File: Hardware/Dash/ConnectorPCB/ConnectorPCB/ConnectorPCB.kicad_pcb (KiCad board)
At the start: 2 copper layers, 44.8 x 43.8 mm, 3 parts, among them J1 776276-1, J2 2.54mm 1x4, J3 2.54mm 1x4

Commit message: PCB R0.1.0
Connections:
- J1 pad 4: CAN_H -> GND
- J1 pad 6: GND -> CAN_H
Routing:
- net GND: track 15.3 -> 26.6 mm
- net CAN_H: track 28.3 -> 29.3 mm
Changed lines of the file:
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@@
       (net 3 "WAKE_UP") (pinfunction "3") (pintype "passive"))
     (pad "4" thru_hole circle (at 2 4) (size 2.625 2.625) (drill 1.75) (layers "*.Cu" "*.Mask")
-      (net 4 "CAN_H") (pinfunction "4") (pintype "passive"))
+      (net 6 "GND") (pinfunction "4") (pintype "passive"))
     (pad "5" thru_hole circle (at 6 4) (size 2.625 2.625) (drill 1.75) (layers "*.Cu" "*.Mask")
       (net 5 "CAN_L") (pinfunction "5") (pintype "passive"))
     (pad "6" thru_hole circle (at 0 8) (size 2.625 2.625) (drill 1.75) (layers "*.Cu" "*.Mask")
-      (net 6 "GND") (pinfunction "6") (pintype "passive"))
+      (net 4 "CAN_H") (pinfunction "6") (pintype "passive"))
     (pad "7" thru_hole circle (at 4 8) (size 2.625 2.625) (drill 1.75) (layers "*.Cu" "*.Mask")
       (net 7 "D+") (pinfunction "7") (pintype "passive"))
@@
     (stroke (width 0.1) (type default)) (layer "Edge.Cuts"))
   (segment (start 141.275 58.925) (end 141.7 58.5) (width 0.8) (layer "F.Cu") (net 1))
-  (segment (start 141.275 73.755) (end 141.275 58.925) (width 0.8) (layer "F.Cu") (net 1))
+  (segment (start 141.275 73.755) (end 141.275 58.925) (width 1.5) (layer "F.Cu") (net 1))
   (segment (start 144.24 71.74) (end 144.24 58.5) (width 0.8) (layer "F.Cu") (net 2))
   (segment (start 144.25 71.75) (end 144.24 71.74) (width 0.8) (layer "F.Cu") (net 2))
@@
   (segment (start 149.275 73.755) (end 146.75 71.23) (width 0.8) (layer "F.Cu") (net 3))
   (segment (start 146.75 71.23) (end 146.75 70) (width 0.8) (layer "F.Cu") (net 3))
-  (segment (start 145.75 64) (end 145.75 62.07) (width 0.8) (layer "B.Cu") (net 4))
-  (segment (start 143.275 77.755) (end 141.801472 77.755) (width 0.8) (layer "B.Cu") (net 4))
-  (segment (start 137.75 75.5) (end 137.75 72) (width 0.8) (layer "B.Cu") (net 4))
-  (segment (start 138.5 76.25) (end 137.75 75.5) (width 0.8) (layer "B.Cu") (net 4))
-  (segment (start 141.801472 77.755) (end 140.296472 76.25) (width 0.8) (layer "B.Cu") (net 4))
-  (segment (start 140.296472 76.25) (end 138.5 76.25) (width 0.8) (layer "B.Cu") (net 4))
-  (segment (start 137.75 72) (end 145.75 64) (width 0.8) (layer "B.Cu") (net 4))
-  (segment (start 145.75 62.07) (end 149.32 58.5) (width 0.8) (layer "B.Cu") (net 4))
+  (segment (start 141.42 81.9) (end 141.275 81.755) (width 0.8) (layer "F.Cu") (net 4))
+  (segment (start 138.225 78.705) (end 138.225 69.595) (width 0.8) (layer "B.Cu") (net 4))
+  (segment (start 141.275 81.755) (end 138.225 78.705) (width 0.8) (layer "B.Cu") (net 4))
+  (segment (start 138.225 69.595) (end 149.32 58.5) (width 0.8) (layer "B.Cu") (net 4))
   (segment (start 152 81.1675) (end 152 94.04) (width 0.8) (layer "F.Cu") (net 5))
   (segment (start 147.275 77.755) (end 148.5875 77.755) (width 0.8) (layer "F.Cu") (net 5))
   (segment (start 152 94.04) (end 149.04 97) (width 0.8) (layer "F.Cu") (net 5))
   (segment (start 148.5875 77.755) (end 152 81.1675) (width 0.8) (layer "F.Cu") (net 5))
-  (segment (start 141.42 81.9) (end 141.275 81.755) (width 0.8) (layer "F.Cu") (net 6))
-  (segment (start 141.42 97) (end 141.42 81.9) (width 0.8) (layer "F.Cu") (net 6))
+  (segment (start 141.42 93.17) (end 141.42 97) (width 1.5) (layer "F.Cu") (net 6))
+  (segment (start 138.645 77.755) (end 136.75 79.65) (width 1.5) (layer "F.Cu") (net 6))
+  (segment (start 136.75 79.65) (end 136.75 88.5) (width 1.5) (layer "F.Cu") (net 6))
+  (segment (start 143.275 77.755) (end 138.645 77.755) (width 1.5) (layer "F.Cu") (net 6))
+  (segment (start 136.75 88.5) (end 141.42 93.17) (width 1.5) (layer "F.Cu") (net 6))
   (via (at 145.5 69) (size 0.5) (drill 0.3) (layers "F.Cu" "B.Cu") (free) (net 6))
   (via (at 149.5 89.25) (size 0.5) (drill 0.3) (layers "F.Cu" "B.Cu") (free) (net 6))

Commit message: :adhesive_bandage: Minor change to the PCB
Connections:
- J2 pad 4: CAN_H -> GND
- J3 pad 4: GND -> CAN_H
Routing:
- net CAN_H: track 29.3 -> 15.5 mm
- net GND: track 26.6 -> 30.5 mm
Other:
- outline, holes or cut-outs redrawn
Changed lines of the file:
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@@
       (net 3 "WAKE_UP") (pintype "passive"))
     (pad "4" thru_hole oval (at 0 -7.62 270) (size 1.7 1.7) (drill 1) (layers "*.Cu" "*.Mask")
-      (net 4 "CAN_H") (pintype "passive"))
+      (net 6 "GND") (pintype "passive"))
     (model "${KICAD6_3DMODEL_DIR}/Connector_PinHeader_2.54mm.3dshapes/PinHeader_1x04_P2.54mm_Vertical.wrl"
       (offset (xyz 0 0 0))
@@
       (net 7 "D+") (pintype "passive"))
     (pad "4" thru_hole oval (at 0 -7.62 90) (size 1.7 1.7) (drill 1) (layers "*.Cu" "*.Mask")
-      (net 6 "GND") (pintype "passive"))
+      (net 4 "CAN_H") (pintype "passive"))
     (model "${KICAD6_3DMODEL_DIR}/Connector_PinHeader_2.54mm.3dshapes/PinHeader_1x04_P2.54mm_Vertical.wrl"
       (offset (xyz 0 0 0))
@@
     )
   )
-  (gr_line (start 122.75 95.5) (end 122.75 60)
+  (gr_arc (start 154.75 60) (mid 153.335786 59.414214) (end 152.75 58)
     (stroke (width 0.1) (type default)) (layer "Edge.Cuts"))
-  (gr_line (start 138.25 56) (end 152.75 56)
+  (gr_line (start 122.75 93.5) (end 122.75 62)
     (stroke (width 0.1) (type default)) (layer "Edge.Cuts"))
-  (gr_line (start 138 95.5) (end 122.75 95.5)
+  (gr_arc (start 167.5 93.5) (mid 166.914214 94.914214) (end 165.5 95.5)
     (stroke (width 0.1) (type default)) (layer "Edge.Cuts"))
-  (gr_line (start 152.75 56) (end 152.75 60)
+  (gr_line (start 140.25 56) (end 150.75 56)
     (stroke (width 0.1) (type default)) (layer "Edge.Cuts"))
-  (gr_line (start 167.5 95.5) (end 167.5 60)
+  (gr_arc (start 138.25 58) (mid 138.835786 56.585786) (end 140.25 56)
     (stroke (width 0.1) (type default)) (layer "Edge.Cuts"))
-  (gr_line (start 152.75 60) (end 167.5 60)
+  (gr_arc (start 152.5 97.75) (mid 151.914214 99.164214) (end 150.5 99.75)
     (stroke (width 0.1) (type default)) (layer "Edge.Cuts"))
-  (gr_line (start 152.5 95.5) (end 167.5 95.5)
+  (gr_arc (start 150.75 56) (mid 152.164214 56.585786) (end 152.75 58)
     (stroke (width 0.1) (type default)) (layer "Edge.Cuts"))
-  (gr_line (start 138.25 60) (end 122.75 60)
+  (gr_arc (start 165.5 60) (mid 166.914214 60.585786) (end 167.5 62)
     (stroke (width 0.1) (type default)) (layer "Edge.Cuts"))
-  (gr_line (start 138 95.5) (end 138 99.75)
+  (gr_arc (start 138.25 58) (mid 137.664214 59.414214) (end 136.25 60)
     (stroke (width 0.1) (type default)) (layer "Edge.Cuts"))
-  (gr_line (start 138.25 60) (end 138.25 56)
+  (gr_line (start 136 95.5) (end 124.75 95.5)
     (stroke (width 0.1) (type default)) (layer "Edge.Cuts"))
-  (gr_line (start 138 99.75) (end 152.5 99.75)
+  (gr_line (start 152.75 58) (end 152.75 58)
     (stroke (width 0.1) (type default)) (layer "Edge.Cuts"))
-  (gr_line (start 152.5 99.75) (end 152.5 95.5)
+  (gr_arc (start 122.75 62) (mid 123.335786 60.585786) (end 124.75 60)
     (stroke (width 0.1) (type default)) (layer "Edge.Cuts"))
-  (segment (start 141.275 58.925) (end 141.7 58.5) (width 0.8) (layer "F.Cu") (net 1))
+  (gr_arc (start 152.5 97.5) (mid 153.085786 96.085786) (end 154.5 95.5)
+    (stroke (width 0.1) (type default)) (layer "Edge.Cuts"))
+  (gr_line (start 167.5 93.5) (end 167.5 62)
+    (stroke (width 0.1) (type default)) (layer "Edge.Cuts"))
+  (gr_line (start 154.75 60) (end 165.5 60)
+    (stroke (width 0.1) (type default)) (layer "Edge.Cuts"))
+  (gr_line (start 154.5 95.5) (end 165.5 95.5)
+    (stroke (width 0.1) (type default)) (layer "Edge.Cuts"))
+  (gr_line (start 136.25 60) (end 124.75 60)
+    (stroke (width 0.1) (type default)) (layer "Edge.Cuts"))
+  (gr_line (start 138 97.5) (end 138 97.75)
+    (stroke (width 0.1) (type default)) (layer "Edge.Cuts"))
+  (gr_arc (start 124.75 95.5) (mid 123.335786 94.914214) (end 122.75 93.5)
+    (stroke (width 0.1) (type default)) (layer "Edge.Cuts"))
+  (gr_line (start 138.25 58) (end 138.25 58)
+    (stroke (width 0.1) (type default)) (layer "Edge.Cuts"))
+  (gr_arc (start 140 99.75) (mid 138.585786 99.164214) (end 138 97.75)
+    (stroke (width 0.1) (type default)) (layer "Edge.Cuts"))
+  (gr_line (start 140 99.75) (end 150.5 99.75)
+    (stroke (width 0.1) (type default)) (layer "Edge.Cuts"))
+  (gr_arc (start 136 95.5) (mid 137.414214 96.085786) (end 138 97.5)
+    (stroke (width 0.1) (type default)) (layer "Edge.Cuts"))
+  (gr_line (start 152.5 97.75) (end 152.5 97.5)
+    (stroke (width 0.1) (type default)) (layer "Edge.Cuts"))
+  (segment (start 141.275 58.925) (end 141.7 58.5) (width 1.5) (layer "F.Cu") (net 1))
   (segment (start 141.275 73.755) (end 141.275 58.925) (width 1.5) (layer "F.Cu") (net 1))
   (segment (start 144.24 71.74) (end 144.24 58.5) (width 0.8) (layer "F.Cu") (net 2))
@@
   (segment (start 149.275 73.755) (end 146.75 71.23) (width 0.8) (layer "F.Cu") (net 3))
   (segment (start 146.75 71.23) (end 146.75 70) (width 0.8) (layer "F.Cu") (net 3))
+  (segment (start 141.275 96.855) (end 141.42 97) (width 0.8) (layer "F.Cu") (net 4))
   (segment (start 141.42 81.9) (end 141.275 81.755) (width 0.8) (layer "F.Cu") (net 4))
-  (segment (start 138.225 78.705) (end 138.225 69.595) (width 0.8) (layer "B.Cu") (net 4))
-  (segment (start 141.275 81.755) (end 138.225 78.705) (width 0.8) (layer "B.Cu") (net 4))
-  (segment (start 138.225 69.595) (end 149.32 58.5) (width 0.8) (layer "B.Cu") (net 4))
+  (segment (start 141.275 81.755) (end 141.275 96.855) (width 0.8) (layer "F.Cu") (net 4))
   (segment (start 152 81.1675) (end 152 94.04) (width 0.8) (layer "F.Cu") (net 5))
   (segment (start 147.275 77.755) (end 148.5875 77.755) (width 0.8) (layer "F.Cu") (net 5))
   (segment (start 152 94.04) (end 149.04 97) (width 0.8) (layer "F.Cu") (net 5))
   (segment (start 148.5875 77.755) (end 152 81.1675) (width 0.8) (layer "F.Cu") (net 5))
-  (segment (start 141.42 93.17) (end 141.42 97) (width 1.5) (layer "F.Cu") (net 6))
-  (segment (start 138.645 77.755) (end 136.75 79.65) (width 1.5) (layer "F.Cu") (net 6))
-  (segment (start 136.75 79.65) (end 136.75 88.5) (width 1.5) (layer "F.Cu") (net 6))
-  (segment (start 143.275 77.755) (end 138.645 77.755) (width 1.5) (layer "F.Cu") (net 6))
-  (segment (start 136.75 88.5) (end 141.42 93.17) (width 1.5) (layer "F.Cu") (net 6))
   (via (at 145.5 69) (size 0.5) (drill 0.3) (layers "F.Cu" "B.Cu") (free) (net 6))
   (via (at 149.5 89.25) (size 0.5) (drill 0.3) (layers "F.Cu" "B.Cu") (free) (net 6))
+  (segment (start 137.755 77.755) (end 136.625 76.625) (width 1.5) (layer "B.Cu") (net 6))
+  (segment (start 141.801472 77.755) (end 137.755 77.755) (width 1.5) (layer "B.Cu") (net 6))
+  (segment (start 136.625 72.525) (end 149.32 59.83) (width 1.5) (layer "B.Cu") (net 6))
+  (segment (start 143.275 77.755) (end 141.801472 77.755) (width 0.8) (layer "B.Cu") (net 6))
+  (segment (start 136.625 76.625) (end 136.625 72.525) (width 1.5) (layer "B.Cu") (net 6))
+  (segment (start 149.32 59.83) (end 149.32 58.5) (width 1.5) (layer "B.Cu") (net 6))
   (segment (start 143.96 97) (end 145.275 95.685) (width 0.8) (layer "F.Cu") (net 7))
   (segment (start 145.275 95.685) (end 145.275 81.755) (width 0.8) (layer "F.Cu") (net 7))

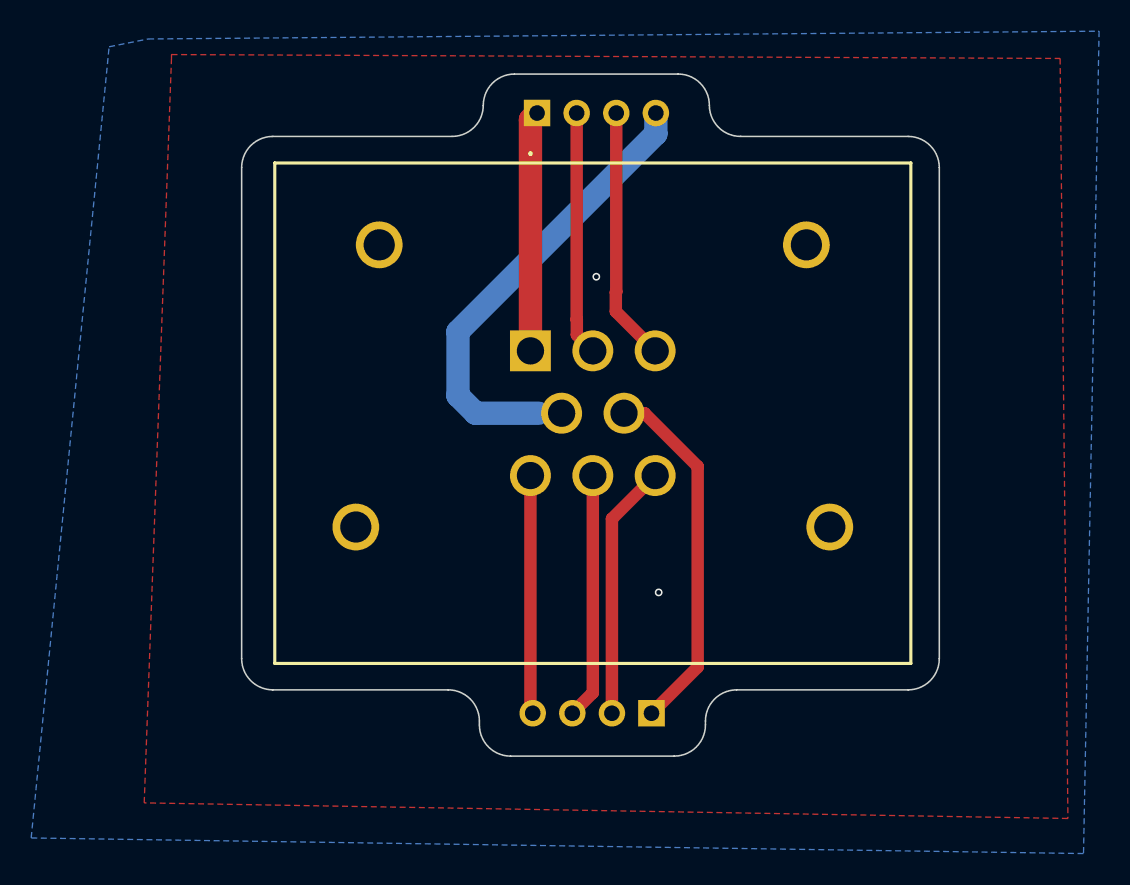
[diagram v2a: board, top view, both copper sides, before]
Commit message: :bug: [FIX] Added space to access the display connector without desoldering the main connector
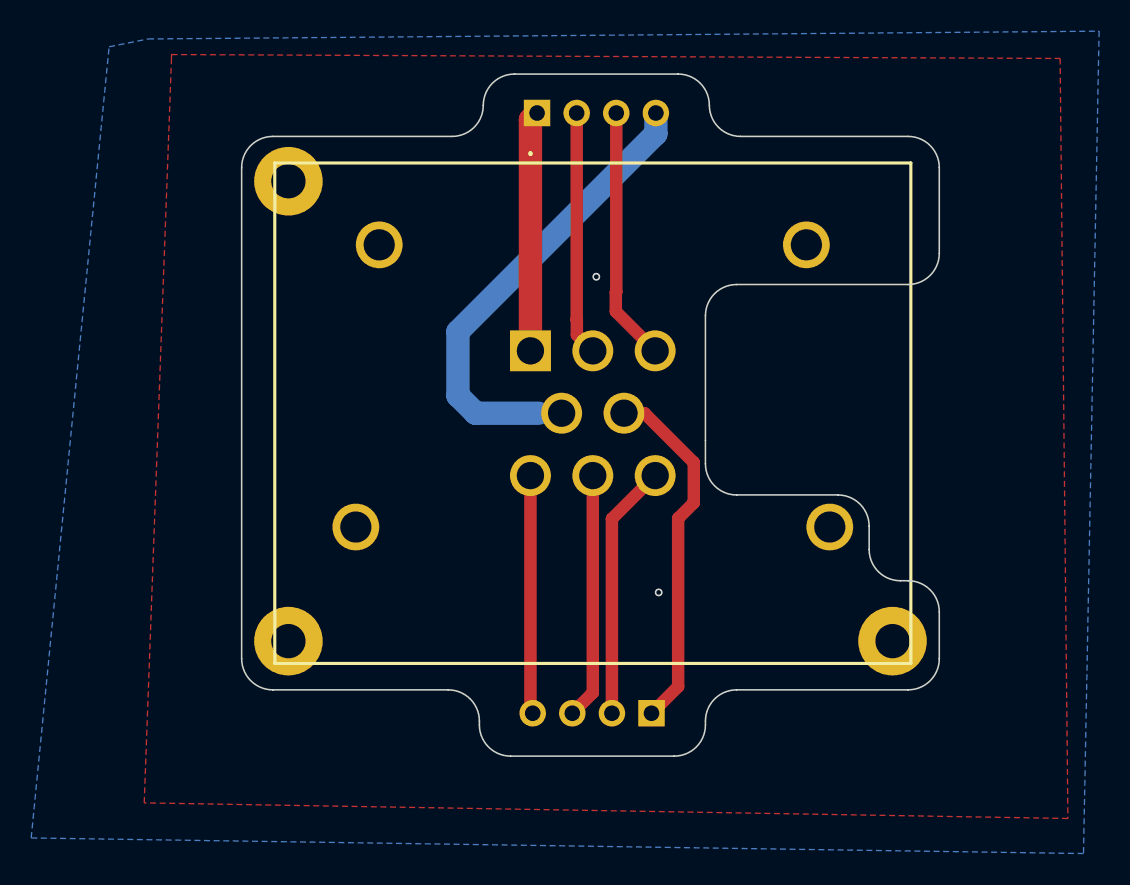
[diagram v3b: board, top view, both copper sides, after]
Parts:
- added ?: , , F.Cu at (164.5, 92.4)
- added ?: , , F.Cu at (125.8, 92.4)
- added H5: MountingHole_Pad, MountingHole:MountingHole_2.2mm_M2_Pad, F.Cu at (125.8, 62.9)
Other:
- outline, holes or cut-outs redrawn
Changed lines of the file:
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@@
     )
+  )
+  (footprint "MountingHole:MountingHole_2.2mm_M2_Pad" (layer "F.Cu")
+    (at 125.75 62.875)
+    (descr "Mounting Hole 2.2mm, M2")
+    (tags "mounting hole 2.2mm m2")
+    (property "LCSC" "C3020128")
+    (property "MOUSER" "")
+    (property "Sheetfile" "connector.kicad_sch")
+    (property "Sheetname" "Connector")
+    (property "ki_description" "Mounting Hole with connection")
+    (property "ki_keywords" "mounting hole")
+    (attr exclude_from_pos_files)
+    (fp_text reference "H5" (at 0 -3.2) (layer "F.SilkS") hide
+        (effects (font (size 1 1) (thickness 0.15)))
+    )
+    (fp_text value "MountingHole_Pad" (at 0 3.2) (layer "F.Fab") hide
+        (effects (font (size 1 1) (thickness 0.15)))
+    )
+    (fp_text user "${REFERENCE}" (at 0 0) (layer "F.Fab")
+        (effects (font (size 1 1) (thickness 0.15)))
+    )
+    (fp_circle (center 0 0) (end 2.2 0)
+      (stroke (width 0.15) (type solid)) (fill none) (layer "Cmts.User"))
+    (fp_circle (center 0 0) (end 2.45 0)
+      (stroke (width 0.05) (type solid)) (fill none) (layer "F.CrtYd"))
+    (pad "1" thru_hole circle (at 0 0) (size 4.4 4.4) (drill 2.2) (layers "*.Cu" "*.Mask")
+      (net 6 "GND") (pinfunction "1") (pintype "input"))
+  )
+  (footprint "" (layer "F.Cu")
+    (at 164.5 92.375)
+    (fp_text reference "" (at 0 0) (layer "F.SilkS")
+        (effects (font (size 1.27 1.27) (thickness 0.15)))
+    )
+    (fp_text value "" (at 0 0) (layer "F.SilkS")
+        (effects (font (size 1.27 1.27) (thickness 0.15)))
+    )
+    (pad "1" thru_hole circle (at 0 0) (size 4.4 4.4) (drill 2.2) (layers "*.Cu" "*.Mask")
+      (net 6 "GND") (pinfunction "1") (pintype "input"))
+  )
+  (footprint "" (layer "F.Cu")
+    (at 125.75 92.375)
+    (fp_text reference "" (at 0 0) (layer "F.SilkS")
+        (effects (font (size 1.27 1.27) (thickness 0.15)))
+    )
+    (fp_text value "" (at 0 0) (layer "F.SilkS")
+        (effects (font (size 1.27 1.27) (thickness 0.15)))
+    )
+    (pad "1" thru_hole circle (at 0 0) (size 4.4 4.4) (drill 2.2) (layers "*.Cu" "*.Mask")
+      (net 6 "GND") (pinfunction "1") (pintype "input"))
   )
   (footprint "Connector_PinHeader_2.54mm:PinHeader_1x04_P2.54mm_Vertical" (layer "B.Cu")
@@
   (gr_arc (start 154.75 60) (mid 153.335786 59.414214) (end 152.75 58)
     (stroke (width 0.1) (type default)) (layer "Edge.Cuts"))
+  (gr_line (start 163 85) (end 163 86.5)
+    (stroke (width 0.1) (type default)) (layer "Edge.Cuts"))
   (gr_line (start 122.75 93.5) (end 122.75 62)
     (stroke (width 0.1) (type default)) (layer "Edge.Cuts"))
@@
   (gr_arc (start 150.75 56) (mid 152.164214 56.585786) (end 152.75 58)
     (stroke (width 0.1) (type default)) (layer "Edge.Cuts"))
+  (gr_line (start 167.5 62) (end 167.5 67.5)
+    (stroke (width 0.1) (type default)) (layer "Edge.Cuts"))
+  (gr_arc (start 161 83) (mid 162.414214 83.585786) (end 163 85)
+    (stroke (width 0.1) (type default)) (layer "Edge.Cuts"))
   (gr_arc (start 165.5 60) (mid 166.914214 60.585786) (end 167.5 62)
     (stroke (width 0.1) (type default)) (layer "Edge.Cuts"))
+  (gr_arc (start 167.5 67.5) (mid 166.914214 68.914214) (end 165.5 69.5)
+    (stroke (width 0.1) (type default)) (layer "Edge.Cuts"))
   (gr_arc (start 138.25 58) (mid 137.664214 59.414214) (end 136.25 60)
     (stroke (width 0.1) (type default)) (layer "Edge.Cuts"))
+  (gr_line (start 165.5 69.5) (end 154.5 69.5)
+    (stroke (width 0.1) (type default)) (layer "Edge.Cuts"))
   (gr_line (start 136 95.5) (end 124.75 95.5)
     (stroke (width 0.1) (type default)) (layer "Edge.Cuts"))
+  (gr_arc (start 165 88.5) (mid 163.585786 87.914214) (end 163 86.5)
+    (stroke (width 0.1) (type default)) (layer "Edge.Cuts"))
+  (gr_line (start 167.5 90.5) (end 167.5 93.5)
+    (stroke (width 0.1) (type default)) (layer "Edge.Cuts"))
   (gr_line (start 152.75 58) (end 152.75 58)
     (stroke (width 0.1) (type default)) (layer "Edge.Cuts"))
   (gr_arc (start 122.75 62) (mid 123.335786 60.585786) (end 124.75 60)
     (stroke (width 0.1) (type default)) (layer "Edge.Cuts"))
+  (gr_arc (start 154.5 83) (mid 153.085786 82.414214) (end 152.5 81)
+    (stroke (width 0.1) (type default)) (layer "Edge.Cuts"))
   (gr_arc (start 152.5 97.5) (mid 153.085786 96.085786) (end 154.5 95.5)
     (stroke (width 0.1) (type default)) (layer "Edge.Cuts"))
-  (gr_line (start 167.5 93.5) (end 167.5 62)
-    (stroke (width 0.1) (type default)) (layer "Edge.Cuts"))
   (gr_line (start 154.75 60) (end 165.5 60)
     (stroke (width 0.1) (type default)) (layer "Edge.Cuts"))
@@
   (gr_arc (start 124.75 95.5) (mid 123.335786 94.914214) (end 122.75 93.5)
     (stroke (width 0.1) (type default)) (layer "Edge.Cuts"))
+  (gr_line (start 152.5 71.5) (end 152.5 79.5)
+    (stroke (width 0.1) (type default)) (layer "Edge.Cuts"))
+  (gr_line (start 152.5 79.5) (end 152.5 81)
+    (stroke (width 0.1) (type default)) (layer "Edge.Cuts"))
+  (gr_arc (start 152.5 71.5) (mid 153.085786 70.085786) (end 154.5 69.5)
+    (stroke (width 0.1) (type default)) (layer "Edge.Cuts"))
   (gr_line (start 138.25 58) (end 138.25 58)
     (stroke (width 0.1) (type default)) (layer "Edge.Cuts"))
+  (gr_line (start 165 88.5) (end 165.5 88.5)
+    (stroke (width 0.1) (type default)) (layer "Edge.Cuts"))
   (gr_arc (start 140 99.75) (mid 138.585786 99.164214) (end 138 97.75)
+    (stroke (width 0.1) (type default)) (layer "Edge.Cuts"))
+  (gr_arc (start 165.5 88.5) (mid 166.914214 89.085786) (end 167.5 90.5)
+    (stroke (width 0.1) (type default)) (layer "Edge.Cuts"))
+  (gr_line (start 154.5 83) (end 161 83)
     (stroke (width 0.1) (type default)) (layer "Edge.Cuts"))
   (gr_line (start 140 99.75) (end 150.5 99.75)
@@
   (segment (start 141.42 81.9) (end 141.275 81.755) (width 0.8) (layer "F.Cu") (net 4))
   (segment (start 141.275 81.755) (end 141.275 96.855) (width 0.8) (layer "F.Cu") (net 4))
-  (segment (start 152 81.1675) (end 152 94.04) (width 0.8) (layer "F.Cu") (net 5))
+  (segment (start 151.75 83.5) (end 150.75 84.5) (width 0.8) (layer "F.Cu") (net 5))
+  (segment (start 150.75 95.29) (end 149.04 97) (width 0.8) (layer "F.Cu") (net 5))
   (segment (start 147.275 77.755) (end 148.5875 77.755) (width 0.8) (layer "F.Cu") (net 5))
-  (segment (start 152 94.04) (end 149.04 97) (width 0.8) (layer "F.Cu") (net 5))
-  (segment (start 148.5875 77.755) (end 152 81.1675) (width 0.8) (layer "F.Cu") (net 5))
+  (segment (start 151.75 80.9175) (end 151.75 83.5) (width 0.8) (layer "F.Cu") (net 5))
+  (segment (start 150.75 84.5) (end 150.75 95.29) (width 0.8) (layer "F.Cu") (net 5))
+  (segment (start 148.5875 77.755) (end 151.75 80.9175) (width 0.8) (layer "F.Cu") (net 5))
   (via (at 145.5 69) (size 0.5) (drill 0.3) (layers "F.Cu" "B.Cu") (free) (net 6))
   (via (at 149.5 89.25) (size 0.5) (drill 0.3) (layers "F.Cu" "B.Cu") (free) (net 6))
